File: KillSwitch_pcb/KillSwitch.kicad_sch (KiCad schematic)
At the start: 24 parts, among them IC1 Wio-SX1262, J1 USB_C_Receptacle_USB2.0, J4 J_ESP_DBG_UART, SW1 SW_RESET, SW10 ARM, SW2 SW_BOOT, SW4 SW_DIP_x08, U1 ESP32-S3-WROOM-1

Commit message: add pullups for i2c, reannotate, update footprints
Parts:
- added R2, R3: 2K2, Resistor_SMD:R_0805_2012Metric_Pad1.20x1.40mm_HandSolder, symbol Device:R_Small
- renumbered C10 to C1, C1 to C2, C8 to C3, C2 to C4, D4 to D1, J4 to J1, J1 to J2, R3 to R1, R12 to R6, R2 to R7, R7 to R9, SW4 to SW1, SW1 to SW2, SW2 to SW3, SW10 to SW4
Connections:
- net +3.3v_ESP: now also R2.1, R3.1
- net KillSwitchIO/SCK: now also R2.2
- net KillSwitchIO/SDA: now also R3.2

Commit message: update płytki: Routing bez GND plus obrys bez zaokrągleń i przycięć
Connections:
- net USB2_N is gone; now on net ESP_USB2_N: U1.13 (USB_D-)
- net USB2_P is gone; now on net ESP_USB2_P: U1.14 (USB_D+)
- net +LORA_PWR renamed +3.3v_LoRa
- net UART_RX: no longer names the net of U1.11 (IO18)
- net UART_TX: no longer names the net of U1.10 (IO17)
- no-connect marks 7 -> 14
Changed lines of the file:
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@@
+	)
+	(junction
+		(at 55.88 60.96)
+		(diameter 0)
+		(color 0 0 0 0)
 	)
 	(junction
@@
 		(diameter 0)
 		(color 0 0 0 0)
+	)
+	(no_connect
+		(at 156.21 69.85)
 	)
 	(no_connect
@@
 	)
 	(no_connect
+		(at 166.37 36.83)
+	)
+	(no_connect
 		(at 125.73 44.45)
+	)
+	(no_connect
+		(at 156.21 72.39)
+	)
+	(no_connect
+		(at 125.73 57.15)
 	)
 	(no_connect
@@
 	)
 	(no_connect
+		(at 125.73 39.37)
+	)
+	(no_connect
 		(at 247.65 62.23)
 	)
+	(no_connect
+		(at 166.37 39.37)
+	)
+	(no_connect
+		(at 156.21 77.47)
+	)
 	(wire
 		(pts
@@
 		(pts
 			(xy 107.95 68.58) (xy 107.95 67.31)
+		)
+		(stroke
+			(width 0)
+			(type default)
+		)
+	)
+	(wire
+		(pts
+			(xy 90.17 63.5) (xy 90.17 69.85)
 		)
 		(stroke
@@
 		)
 	)
-	(label "UART_TX"
-		(at 157.48 36.83 0)
-		(effects
-			(font
-				(size 1.27 1.27)
-			)
-			(justify left bottom)
-		)
-	)
 	(label "+3.3v_ESP"
 		(at 105.41 114.3 180)
@@
 		)
 	)
-	(label "UART_RX"
-		(at 157.48 39.37 0)
-		(effects
-			(font
-				(size 1.27 1.27)
-			)
-			(justify left bottom)
-		)
-	)
 	(label "ESP_USB2_P"
 		(at 265.43 49.53 0)
@@
 		)
 	)
+	(label "+3.3v_ESP"
+		(at 90.17 63.5 180)
+		(effects
+			(font
+				(size 1.27 1.27)
+			)
+			(justify right bottom)
+		)
+	)
+	(label "ESP_USB2_P"
+		(at 166.37 44.45 0)
+		(effects
+			(font
+				(size 1.27 1.27)
+			)
+			(justify left bottom)
+		)
+	)
 	(label "ESP_USB2_N"
 		(at 265.43 46.99 0)
@@
 		)
 	)
+	(label "ESP_USB2_N"
+		(at 166.37 41.91 0)
+		(effects
+			(font
+				(size 1.27 1.27)
+			)
+			(justify left bottom)
+		)
+	)
 	(label "DIP_SEL7"
 		(at 156.21 46.99 0)
@@
 			)
 			(justify right bottom)
-		)
-	)
-	(hierarchical_label "UART_TX"
-		(shape output)
-		(at 166.37 36.83 0)
-		(effects
-			(font
-				(size 1.27 1.27)
-			)
-			(justify left)
-		)
-	)
-	(hierarchical_label "USB2_N"
-		(shape bidirectional)
-		(at 166.37 41.91 0)
-		(effects
-			(font
-				(size 1.27 1.27)
-			)
-			(justify left)
-		)
-	)
-	(hierarchical_label "USB2_P"
-		(shape bidirectional)
-		(at 166.37 44.45 0)
-		(effects
-			(font
-				(size 1.27 1.27)
-			)
-			(justify left)
-		)
-	)
-	(hierarchical_label "+LORA_PWR"
-		(shape input)
-		(at 57.15 26.67 0)
-		(effects
-			(font
-				(size 1.27 1.27)
-			)
-			(justify left)
-		)
-	)
-	(hierarchical_label "UART_RX"
-		(shape input)
-		(at 166.37 39.37 0)
-		(effects
-			(font
-				(size 1.27 1.27)
-			)
-			(justify left)
 		)
 	)
@@
 					(unit 1)
 				)
+			)
+		)
+	)
+	(symbol
+		(lib_id "power:PWR_FLAG")
+		(at 55.88 60.96 90)
+		(unit 1)
+		(exclude_from_sim no)
+		(in_bom yes)
+		(on_board yes)
+		(dnp no)
+		(fields_autoplaced yes)
+		(property "Reference" "#FLG02"
+			(at 53.975 60.96 0)
+			(effects
+				(font
+					(size 1.27 1.27)
+				)
+				(hide yes)
+			)
+		)
+		(property "Value" "PWR_FLAG"
+			(at 52.07 60.9599 90)
+			(effects
+				(font
+					(size 1.27 1.27)
+				)
+				(justify left)
+			)
+		)
+		(property "Footprint" ""
+			(at 55.88 60.96 0)
+			(effects
+				(font
+					(size 1.27 1.27)
+				)
+				(hide yes)
+			)
+		)
+		(property "Datasheet" "~"
+			(at 55.88 60.96 0)
+			(effects
+				(font
+					(size 1.27 1.27)
+				)
+				(hide yes)
+			)
+		)
+		(property "Description" "Special symbol for telling ERC where power comes from"
+			(at 55.88 60.96 0)
+			(effects
+				(font
+					(size 1.27 1.27)
+				)
+				(hide yes)
+			)
+		)
+		(pin "1"
+		)
+		(instances
+			(project ""
+				(path "/722d8df3-08e9-470c-940d-01bb552f6a6b"
+					(reference "#FLG02")
+					(unit 1)
+				)

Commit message: końcowa werjsa
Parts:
- added D19: Amber, LED_THT:LED_Rectangular_W5.0mm_H2.0mm, symbol Device:LED_Small_Filled
- added R27: 120R, Resistor_SMD:R_0805_2012Metric_Pad1.20x1.40mm_HandSolder, symbol Device:R_Small
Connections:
- net GND: now also R27.2
- net LED_ARM: now reaches U1.25 (IO48)
- net LED_ARM: now also D19.2 (A)
- new net: D19.1 (K), R27.1
- no-connect marks 14 -> 13
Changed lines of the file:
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@@
 		(at 166.37 39.37)
 	)
-	(no_connect
-		(at 156.21 77.47)
-	)
 	(wire
 		(pts
@@
 	(wire
 		(pts
+			(xy 184.15 77.47) (xy 184.15 78.74)
+		)
+		(stroke
+			(width 0)
+			(type default)
+		)
+	)
+	(wire
+		(pts
 			(xy 107.95 68.58) (xy 107.95 67.31)
 		)
@@
 	(wire
 		(pts
+			(xy 156.21 77.47) (xy 166.37 77.47)
+		)
+		(stroke
+			(width 0)
+			(type default)
+		)
+	)
+	(wire
+		(pts
 			(xy 109.22 67.31) (xy 110.49 67.31)
 		)
@@
 	(wire
 		(pts
+			(xy 177.8 77.47) (xy 184.15 77.47)
+		)
+		(stroke
+			(width 0)
+			(type default)
+		)
+	)
+	(wire
+		(pts
 			(xy 140.97 82.55) (xy 140.97 88.9)
 		)
@@
 		)
 	)
+	(wire
+		(pts
+			(xy 171.45 77.47) (xy 172.72 77.47)
+		)
+		(stroke
+			(width 0)
+			(type default)
+		)
+	)
 	(label "DIP_SEL3"
 		(at 125.73 64.77 180)
@@
 		)
 	)
+	(label "LED_ARM"
+		(at 160.02 77.47 0)
+		(effects
+			(font
+				(size 1.27 1.27)
+			)
+			(justify left bottom)
+		)
+	)
 	(label "LORA_SPI_CLK"
 		(at 40.64 45.72 180)
@@
 	)
 	(symbol
+		(lib_id "Device:LED_Small_Filled")
+		(at 168.91 77.47 0)
+		(mirror y)
+		(unit 1)
+		(exclude_from_sim no)
+		(in_bom yes)
+		(on_board yes)
+		(dnp no)
+		(property "Reference" "D19"
+			(at 166.37 73.66 0)
+			(effects
+				(font
+					(size 1.27 1.27)
+				)
+				(justify right)
+			)
+		)
+		(property "Value" "Amber"
+			(at 166.37 71.12 0)
+			(effects
+				(font
+					(size 1.27 1.27)
+				)
+				(justify right)
+			)
+		)
+		(property "Footprint" "LED_THT:LED_Rectangular_W5.0mm_H2.0mm"
+			(at 168.91 77.47 90)
+			(effects
+				(font
+					(size 1.27 1.27)
+				)
+				(hide yes)
+			)
+		)
+		(property "Datasheet" "~"
+			(at 168.91 77.47 90)
+			(effects
+				(font
+					(size 1.27 1.27)
+				)
+				(hide yes)
+			)
+		)
+		(property "Description" ""
+			(at 168.91 77.47 0)
+			(effects
+				(font
+					(size 1.27 1.27)
+				)
+			)
+		)
+		(pin "1"
+		)
+		(pin "2"
+		)
+		(instances
+			(project "KillSwitch"
+				(path "/722d8df3-08e9-470c-940d-01bb552f6a6b"
+					(reference "D19")
+					(unit 1)
+				)
+			)
+		)
+	)
+	(symbol
 		(lib_id "Mechanical:MountingHole")
 		(at 275.59 140.97 0)
@@
 	(symbol
 		(lib_id "power:GND")
+		(at 184.15 78.74 0)
+		(unit 1)
+		(exclude_from_sim no)
+		(in_bom yes)
+		(on_board yes)
+		(dnp no)
+		(property "Reference" "#PWR027"
+			(at 184.15 85.09 0)
+			(effects
+				(font
+					(size 1.27 1.27)
+				)
+				(hide yes)
+			)
+		)
+		(property "Value" "GND"
+			(at 184.15 83.82 0)
+			(effects
+				(font
+					(size 1.27 1.27)
+				)
+			)
+		)
+		(property "Footprint" ""
+			(at 184.15 78.74 0)
+			(effects
+				(font
+					(size 1.27 1.27)
+				)
+				(hide yes)
+			)
+		)
+		(property "Datasheet" ""
+			(at 184.15 78.74 0)
+			(effects
+				(font
+					(size 1.27 1.27)
+				)
+				(hide yes)
+			)
+		)
+		(property "Description" "Power symbol creates a global label with name \"GND\" , ground"
+			(at 184.15 78.74 0)
+			(effects
+				(font
+					(size 1.27 1.27)
+				)
+				(hide yes)
+			)
+		)
+		(pin "1"
+		)
+		(instances
+			(project "KillSwitch"
+				(path "/722d8df3-08e9-470c-940d-01bb552f6a6b"
+					(reference "#PWR027")
+					(unit 1)
+				)
+			)
+		)
+	)
+	(symbol
+		(lib_id "power:GND")
 		(at 67.31 140.97 0)
 		(unit 1)
@@
 					(unit 1)
 				)
+			)
+		)
+	)
+	(symbol
+		(lib_id "Device:R_Small")
+		(at 175.26 77.47 90)
+		(unit 1)
+		(exclude_from_sim no)
+		(in_bom yes)
+		(on_board yes)
+		(dnp no)
+		(property "Reference" "R27"
+			(at 177.8 76.2 90)
+			(effects
+				(font
+					(size 1.27 1.27)
+				)
+				(justify left)
+			)
+		)
+		(property "Value" "120R"
+			(at 179.07 72.39 90)
+			(effects
+				(font
+					(size 1.27 1.27)
+				)
+				(justify left)
+			)
+		)
+		(property "Footprint" "Resistor_SMD:R_0805_2012Metric_Pad1.20x1.40mm_HandSolder"
+			(at 175.26 77.47 0)
+			(effects
+				(font
+					(size 1.27 1.27)
+				)
+				(hide yes)
+			)
+		)
+		(property "Datasheet" "~"
+			(at 175.26 77.47 0)
+			(effects
+				(font
+					(size 1.27 1.27)
+				)
+				(hide yes)
+			)
+		)
+		(property "Description" ""
+			(at 175.26 77.47 0)
+			(effects
+				(font
+					(size 1.27 1.27)
+				)
+			)
+		)
+		(pin "1"
+		)
+		(pin "2"
+		)
+		(instances
+			(project "KillSwitch"
+				(path "/722d8df3-08e9-470c-940d-01bb552f6a6b"
+					(reference "R27")
+					(unit 1)
+				)

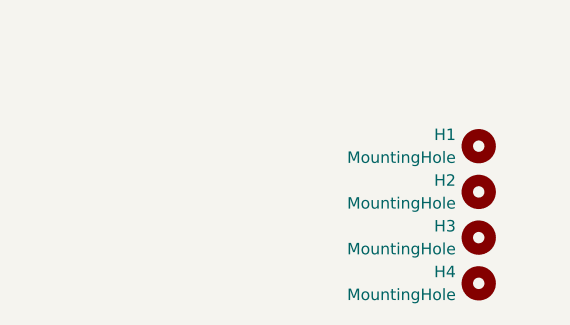
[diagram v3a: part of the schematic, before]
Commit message: Move LEDs resistors to the back side, correct decoupling caps, add aesthetic changes
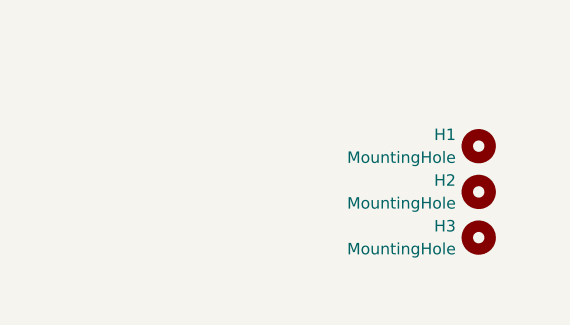
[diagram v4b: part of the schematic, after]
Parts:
- removed H4: MountingHole, MountingHole:MountingHole_3.2mm_M3_DIN965, symbol Mechanical:MountingHole
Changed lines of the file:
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@@
-	)
-	(symbol
-		(lib_id "Mechanical:MountingHole")
-		(at 275.59 156.21 0)
-		(mirror y)
-		(unit 1)
-		(exclude_from_sim no)
-		(in_bom no)
-		(on_board yes)
-		(dnp no)
-		(fields_autoplaced yes)
-		(property "Reference" "H4"
-			(at 273.05 154.9399 0)
-			(effects
-				(font
-					(size 1.27 1.27)
-				)
-				(justify left)
-			)
-		)
-		(property "Value" "MountingHole"
-			(at 273.05 157.4799 0)
-			(effects
-				(font
-					(size 1.27 1.27)
-				)
-				(justify left)
-			)
-		)
-		(property "Footprint" "MountingHole:MountingHole_3.2mm_M3_DIN965"
-			(at 275.59 156.21 0)
-			(effects
-				(font
-					(size 1.27 1.27)
-				)
-				(hide yes)
-			)
-		)
-		(property "Datasheet" "~"
-			(at 275.59 156.21 0)
-			(effects
-				(font
-					(size 1.27 1.27)
-				)
-				(hide yes)
-			)
-		)
-		(property "Description" "Mounting Hole without connection"
-			(at 275.59 156.21 0)
-			(effects
-				(font
-					(size 1.27 1.27)
-				)
-				(hide yes)
-			)
-		)
-		(instances
-			(project "KillSwitch"
-				(path "/722d8df3-08e9-470c-940d-01bb552f6a6b"
-					(reference "H4")
-					(unit 1)
-				)
-			)
-		)
 	)
 	(symbol
